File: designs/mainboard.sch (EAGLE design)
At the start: 11 parts, among them U1 ESP32-DEVKITC-32D

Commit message: changed schematic for display in eagle
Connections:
- new net N$4: U1.IO5
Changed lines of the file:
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@@
 <pinref part="U1" gate="G$1" pin="IO18"/>
 <wire x1="76.2" y1="50.8" x2="81.28" y2="50.8" width="0.1524" layer="91"/>
-<label x="81.28" y="50.8" size="1.778" layer="95"/>
+<label x="22.86" y="55.88" size="1.778" layer="95"/>
 </segment>
 </net>
@@
 <pinref part="U1" gate="G$1" pin="IO19"/>
 <wire x1="76.2" y1="53.34" x2="81.28" y2="53.34" width="0.1524" layer="91"/>
-<label x="81.28" y="53.34" size="1.778" layer="95"/>
+<label x="22.86" y="53.34" size="1.778" layer="95"/>
 </segment>
 </net>
@@
 <segment>
 <pinref part="U1" gate="G$1" pin="IO27"/>
-<label x="22.86" y="45.72" size="1.778" layer="95"/>
+<label x="22.86" y="48.26" size="1.778" layer="95"/>
 <wire x1="35.56" y1="45.72" x2="22.86" y2="45.72" width="0.1524" layer="91"/>
 </segment>
@@
 <segment>
 <pinref part="U1" gate="G$1" pin="IO26"/>
-<label x="22.86" y="48.26" size="1.778" layer="95"/>
+<label x="22.86" y="50.8" size="1.778" layer="95"/>
 <wire x1="35.56" y1="48.26" x2="22.86" y2="48.26" width="0.1524" layer="91"/>
 </segment>
@@
 <pinref part="U1" gate="G$1" pin="CLK"/>
 <wire x1="76.2" y1="25.4" x2="78.74" y2="25.4" width="0.1524" layer="91"/>
-<label x="22.86" y="53.34" size="1.778" layer="95"/>
+<label x="81.28" y="50.8" size="1.778" layer="95"/>
 </segment>
 <segment>
@@
 <pinref part="U1" gate="G$1" pin="SD0"/>
 <wire x1="76.2" y1="27.94" x2="78.74" y2="27.94" width="0.1524" layer="91"/>
-<label x="81.28" y="66.04" size="1.778" layer="95"/>
+<label x="81.28" y="68.58" size="1.778" layer="95"/>
 </segment>
 <segment>
@@
 <pinref part="U1" gate="G$1" pin="SD1"/>
 <wire x1="76.2" y1="30.48" x2="78.74" y2="30.48" width="0.1524" layer="91"/>
-<label x="81.28" y="68.58" size="1.778" layer="95"/>
+<label x="81.28" y="53.34" size="1.778" layer="95"/>
 </segment>
 <segment>
@@
 <pinref part="U1" gate="G$1" pin="IO32"/>
 <wire x1="35.56" y1="55.88" x2="22.86" y2="55.88" width="0.1524" layer="91"/>
-<label x="22.86" y="55.88" size="1.778" layer="95"/>
+<label x="81.28" y="48.26" size="1.778" layer="95"/>
 </segment>
 <segment>
@@
 <segment>
 <pinref part="U1" gate="G$1" pin="IO25"/>
-<label x="22.86" y="50.8" size="1.778" layer="95"/>
+<label x="22.86" y="45.72" size="1.778" layer="95"/>
 <wire x1="35.56" y1="50.8" x2="22.86" y2="50.8" width="0.1524" layer="91"/>
 </segment>
@@
 </segment>
 </net>
+<net name="N$4" class="0">
+<segment>
+<pinref part="U1" gate="G$1" pin="IO5"/>
+<wire x1="76.2" y1="48.26" x2="81.28" y2="48.26" width="0.1524" layer="91"/>
+</segment>
+</net>

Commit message: updated mainboard schematic
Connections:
- new net AUDIO_RX: U1.IO15
- new net AUDIO_TX: U1.IO4
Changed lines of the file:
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@@
+</segment>
+</net>
+<net name="AUDIO_TX" class="0">
+<segment>
+<pinref part="U1" gate="G$1" pin="IO4"/>
+<wire x1="76.2" y1="40.64" x2="81.28" y2="40.64" width="0.1524" layer="91"/>
+<label x="81.28" y="40.64" size="1.778" layer="95"/>
+</segment>
+</net>
+<net name="AUDIO_RX" class="0">
+<segment>
+<pinref part="U1" gate="G$1" pin="IO15"/>
+<wire x1="76.2" y1="33.02" x2="81.28" y2="33.02" width="0.1524" layer="91"/>
+<label x="81.28" y="33.02" size="1.778" layer="95"/>
 </segment>
 </net>

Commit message: added Library for DFPlayerMini
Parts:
- added U2: ESP32-DEVKITC-32D, ESP32-DEVKITC-32D_2:ESP32-DEVKITC-32D
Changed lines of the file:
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@@
 <grid distance="0.1" unitdist="inch" unit="inch" style="lines" multiple="1" display="no" altdistance="0.01" altunitdist="inch" altunit="inch"/>
 <layers>
-<layer number="1" name="Top" color="4" fill="1" visible="no" active="no"/>
-<layer number="2" name="Route2" color="1" fill="3" visible="no" active="no"/>
-<layer number="3" name="Route3" color="4" fill="3" visible="no" active="no"/>
-<layer number="4" name="tKeepout" color="0" fill="1" visible="no" active="no"/>
-<layer number="5" name="Route5" color="4" fill="4" visible="no" active="no"/>
-<layer number="6" name="Route6" color="1" fill="8" visible="no" active="no"/>
-<layer number="7" name="Route7" color="4" fill="8" visible="no" active="no"/>
-<layer number="8" name="Route8" color="1" fill="2" visible="no" active="no"/>
-<layer number="9" name="Route9" color="4" fill="2" visible="no" active="no"/>
-<layer number="10" name="Route10" color="1" fill="7" visible="no" active="no"/>
-<layer number="11" name="Route11" color="4" fill="7" visible="no" active="no"/>
-<layer number="12" name="Route12" color="1" fill="5" visible="no" active="no"/>
-<layer number="13" name="Route13" color="4" fill="5" visible="no" active="no"/>
-<layer number="14" name="Route14" color="1" fill="6" visible="no" active="no"/>
-<layer number="15" name="Route15" color="4" fill="6" visible="no" active="no"/>
-<layer number="16" name="Bottom" color="1" fill="1" visible="no" active="no"/>
-<layer number="17" name="Pads" color="2" fill="1" visible="no" active="no"/>
-<layer number="18" name="Vias" color="2" fill="1" visible="no" active="no"/>
-<layer number="19" name="Unrouted" color="6" fill="1" visible="no" active="no"/>
-<layer number="20" name="Dimension" color="15" fill="1" visible="no" active="no"/>
-<layer number="21" name="tPlace" color="7" fill="1" visible="no" active="no"/>
-<layer number="22" name="bPlace" color="7" fill="1" visible="no" active="no"/>
-<layer number="23" name="tOrigins" color="15" fill="1" visible="no" active="no"/>
-<layer number="24" name="bOrigins" color="15" fill="1" visible="no" active="no"/>
-<layer number="25" name="tNames" color="7" fill="1" visible="no" active="no"/>
-<layer number="26" name="bNames" color="7" fill="1" visible="no" active="no"/>
-<layer number="27" name="tValues" color="7" fill="1" visible="no" active="no"/>
-<layer number="28" name="bValues" color="7" fill="1" visible="no" active="no"/>
+<layer number="1" name="Top" color="4" fill="1" visible="yes" active="no"/>
+<layer number="2" name="Route2" color="1" fill="3" visible="yes" active="no"/>
+<layer number="3" name="Route3" color="4" fill="3" visible="yes" active="no"/>
+<layer number="4" name="tKeepout" color="0" fill="1" visible="yes" active="no"/>
+<layer number="5" name="Route5" color="4" fill="4" visible="yes" active="no"/>
+<layer number="6" name="Route6" color="1" fill="8" visible="yes" active="no"/>
+<layer number="7" name="Route7" color="4" fill="8" visible="yes" active="no"/>
+<layer number="8" name="Route8" color="1" fill="2" visible="yes" active="no"/>
+<layer number="9" name="Route9" color="4" fill="2" visible="yes" active="no"/>
+<layer number="10" name="Route10" color="1" fill="7" visible="yes" active="no"/>
+<layer number="11" name="Route11" color="4" fill="7" visible="yes" active="no"/>
+<layer number="12" name="Route12" color="1" fill="5" visible="yes" active="no"/>
+<layer number="13" name="Route13" color="4" fill="5" visible="yes" active="no"/>
+<layer number="14" name="Route14" color="1" fill="6" visible="yes" active="no"/>
+<layer number="15" name="Route15" color="4" fill="6" visible="yes" active="no"/>
+<layer number="16" name="Bottom" color="1" fill="1" visible="yes" active="no"/>
+<layer number="17" name="Pads" color="2" fill="1" visible="yes" active="no"/>
+<layer number="18" name="Vias" color="2" fill="1" visible="yes" active="no"/>
+<layer number="19" name="Unrouted" color="6" fill="1" visible="yes" active="no"/>
+<layer number="20" name="Dimension" color="15" fill="1" visible="yes" active="no"/>
+<layer number="21" name="tPlace" color="7" fill="1" visible="yes" active="no"/>
+<layer number="22" name="bPlace" color="7" fill="1" visible="yes" active="no"/>
+<layer number="23" name="tOrigins" color="15" fill="1" visible="yes" active="no"/>
+<layer number="24" name="bOrigins" color="15" fill="1" visible="yes" active="no"/>
+<layer number="25" name="tNames" color="7" fill="1" visible="yes" active="no"/>
+<layer number="26" name="bNames" color="7" fill="1" visible="yes" active="no"/>
+<layer number="27" name="tValues" color="7" fill="1" visible="yes" active="no"/>
+<layer number="28" name="bValues" color="7" fill="1" visible="yes" active="no"/>
 <layer number="29" name="tStop" color="7" fill="3" visible="no" active="no"/>
 <layer number="30" name="bStop" color="7" fill="6" visible="no" active="no"/>
@@
 <layer number="35" name="tGlue" color="7" fill="4" visible="no" active="no"/>
 <layer number="36" name="bGlue" color="7" fill="5" visible="no" active="no"/>
-<layer number="37" name="tTest" color="7" fill="1" visible="no" active="no"/>
-<layer number="38" name="bTest" color="7" fill="1" visible="no" active="no"/>
+<layer number="37" name="tTest" color="7" fill="1" visible="yes" active="no"/>
+<layer number="38" name="bTest" color="7" fill="1" visible="yes" active="no"/>
 <layer number="39" name="tKeepout" color="4" fill="11" visible="no" active="no"/>
 <layer number="40" name="bKeepout" color="1" fill="11" visible="no" active="no"/>
@@
 <layer number="44" name="Drills" color="7" fill="1" visible="no" active="no"/>
 <layer number="45" name="Holes" color="7" fill="1" visible="no" active="no"/>
-<layer number="46" name="Milling" color="3" fill="1" visible="no" active="no"/>
-<layer number="47" name="Measures" color="7" fill="1" visible="no" active="no"/>
-<layer number="48" name="Document" color="7" fill="1" visible="no" active="no"/>
-<layer number="49" name="Reference" color="7" fill="1" visible="no" active="no"/>
-<layer number="51" name="tDocu" color="7" fill="1" visible="no" active="no"/>
-<layer number="52" name="bDocu" color="7" fill="1" visible="no" active="no"/>
+<layer number="46" name="Milling" color="3" fill="1" visible="yes" active="no"/>
+<layer number="47" name="Measures" color="7" fill="1" visible="yes" active="no"/>
+<layer number="48" name="Document" color="7" fill="1" visible="yes" active="no"/>
+<layer number="49" name="Reference" color="7" fill="1" visible="yes" active="no"/>
+<layer number="51" name="tDocu" color="7" fill="1" visible="yes" active="no"/>
+<layer number="52" name="bDocu" color="7" fill="1" visible="yes" active="no"/>
 <layer number="88" name="SimResults" color="9" fill="1" visible="yes" active="yes"/>
 <layer number="89" name="SimProbes" color="9" fill="1" visible="yes" active="yes"/>
@@
 <part name="R6" library="rcl" library_urn="urn:adsk.eagle:library:334" deviceset="R-EU_" device="0204/7" package3d_urn="urn:adsk.eagle:package:23498/2" value="1k"/>
 <part name="SV1" library="con-lstb" library_urn="urn:adsk.eagle:library:162" deviceset="MA13-1" device="" package3d_urn="urn:adsk.eagle:package:8367/1"/>
+<part name="U2" library="ESP32-DEVKITC-32D_2" deviceset="ESP32-DEVKITC-32D" device="">
+<attribute name="SPICEPREFIX" value="X"/>
+</part>
 </parts>
 <sheets>
@@
 <attribute name="NAME" x="-19.05" y="41.402" size="1.778" layer="95"/>
 </instance>
+<instance part="U2" gate="G$1" x="-88.9" y="109.22" smashed="yes"/>
 </instances>
 <busses>

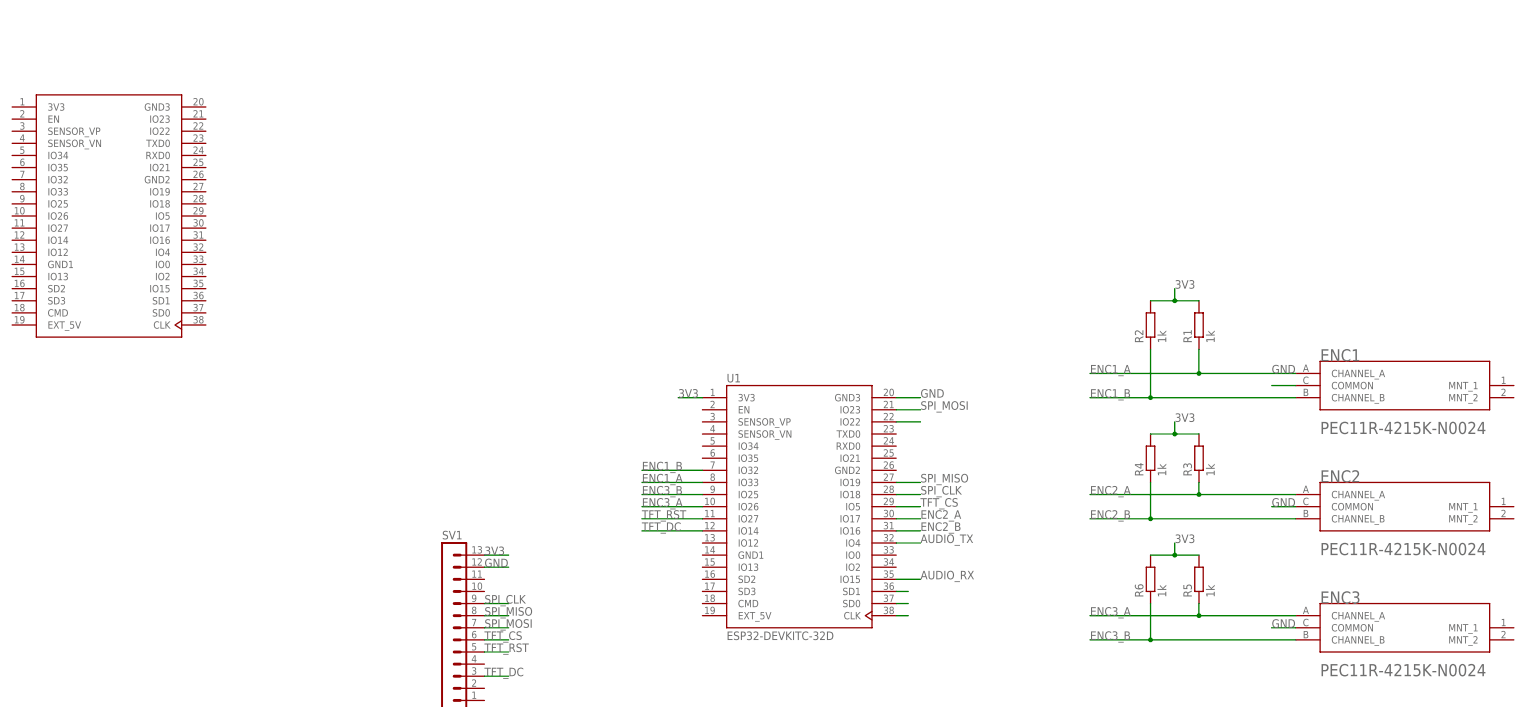
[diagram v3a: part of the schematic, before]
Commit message: added DFPlayer to mainboard schematic
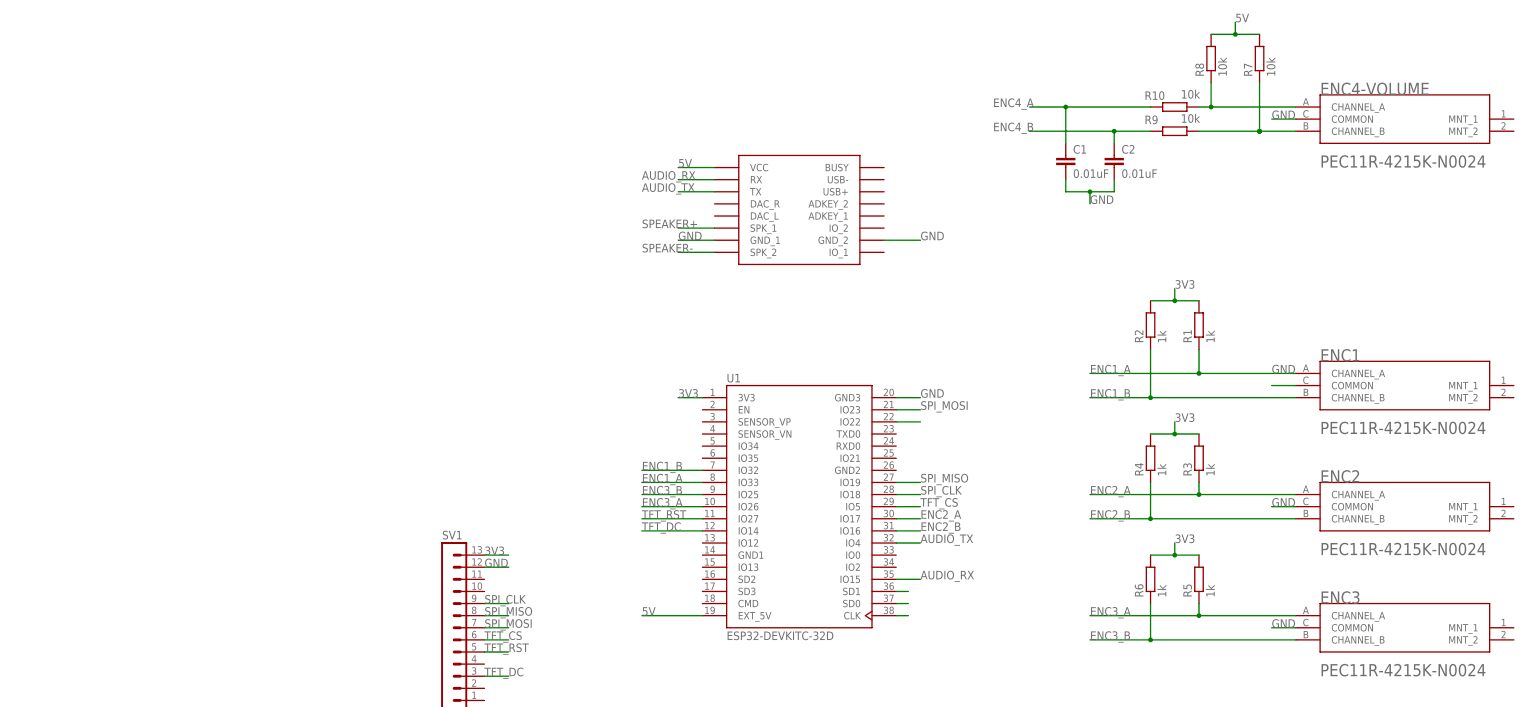
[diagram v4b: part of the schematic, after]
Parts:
- removed U2: ESP32-DEVKITC-32D, ESP32-DEVKITC-32D_2:ESP32-DEVKITC-32D
- added C1, C2: 0.01uF, capacitor-wima:C2,5-3
- added ENC4-VOLUME: BOURNS_PEC11R-4215K-N0024BOURNS_PEC11R-4215K-N0024_0_0, Bourns - PEC11R-4215K-N0024:BOURNS_PEC11R-4215K-N0024BOURNS_PEC11R-4215K-N0024_0_0
- added R10, R7, R8, R9: 10k, rcl:R-EU_0204/7
- added U$1: DFPLAYER, DFPlayer_v1:DFPLAYER
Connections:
- new net 5V: R7.2, R8.2, U$1.VCC, U1.EXT_5V
- new net ENC4_A: C1.1, R10.1
- new net ENC4_B: C2.1, R9.1
- new net N$5: ENC4-VOLUME.CHANNEL_A, R10.2, R8.1
- new net N$6: ENC4-VOLUME.CHANNEL_B, R7.1, R9.2
- new net SPEAKER+: U$1.SPK_1
- new net SPEAKER-: U$1.SPK_2
- net AUDIO_RX: now also U$1.RX
- net AUDIO_TX: now also U$1.TX
- net GND: now also C1.2, C2.2, ENC4-VOLUME.COMMON, U$1.GND_1, U$1.GND_2

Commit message: added additional encoders and connected them to the ESP
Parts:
- removed ENC1, ENC2, ENC3: BOURNS_PEC11R-4215K-N0024BOURNS_PEC11R-4215K-N0024_0_0, Bourns - PEC11R-4215K-N0024:BOURNS_PEC11R-4215K-N0024BOURNS_PEC11R-4215K-N0024_0_0
- added C10, C3, C4, C5, C6, C7, C8, C9: 0.01uF, capacitor-wima:C2,5-3
- added ENCODER1, ENCODER2, ENCODER3, ENCODER_ANTENNA: BOURNS_PEC11R-4215K-N0024BOURNS_PEC11R-4215K-N0024_0_0, Bourns - PEC11R-4215K-N0024:BOURNS_PEC11R-4215K-N0024BOURNS_PEC11R-4215K-N0024_0_0
- added R11, R12, R13, R14, R15, R16, R17, R18, R19, R20: 10k, rcl:R-EU_0204/7
- R1, R2, R3, R4, R5, R6: value 1k -> 10k
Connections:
- removed net ENC4_A: C1.1, R10.1
- removed net ENC4_B: C2.1, R9.1
- new net 3.3V: R1.2, R13.2, R14.2, R17.2, R18.2, R2.2, R3.2, R4.2, R7.2, R8.2
- new net ENCVOL_A: C1.1, R10.1, U1.IO22
- new net ENCVOL_B: C2.1, R9.1, U1.IO21
- new net ENC_ANT_A: C9.1, R6.1, U1.IO35
- new net ENC_ANT_B: C10.1, R5.1, U1.IO34
- new net N$11: ENCODER1.CHANNEL_A, R14.1, R16.2
- new net N$12: ENCODER1.CHANNEL_B, R13.1, R15.2
- new net N$14: ENCODER3.CHANNEL_A, R18.1, R20.2
- new net N$15: ENCODER3.CHANNEL_B, R17.1, R19.2
- new net N$17: ENCODER_ANTENNA.CHANNEL_B, R3.1, R5.2
- net 3V3: no longer R5.2, R6.2
- net 5V: no longer R7.2, R8.2
- net ENC1_A: now also C3.1, R16.1; no longer ENC1.CHANNEL_A, R1.1
- net ENC1_B: now also C4.1, R15.1; no longer ENC1.CHANNEL_B, R2.1
- net ENC2_A: now also C5.1, R12.1; no longer ENC2.CHANNEL_A, R3.1
- net ENC2_B: now also C6.1, R11.1; no longer ENC2.CHANNEL_B, R4.1
- net ENC3_A: now also C7.1, R20.1; no longer ENC3.CHANNEL_A, R5.1
- net ENC3_B: now also C8.1, R19.1; no longer ENC3.CHANNEL_B, R6.1
- net GND: now also C10.2, C3.2, C4.2, C5.2, C6.2, C7.2, C8.2, C9.2, ENCODER1.COMMON, ENCODER2.COMMON, ENCODER3.COMMON, ENCODER_ANTENNA.COMMON; no longer ENC1.COMMON, ENC2.COMMON, ENC3.COMMON
- net N$2: now also ENCODER2.CHANNEL_A, R12.2, R2.1; no longer U1.IO22
- net N$8: now also ENCODER_ANTENNA.CHANNEL_A, R4.1, R6.2; no longer R3.2, R4.2
- net N$9: now also ENCODER2.CHANNEL_B, R1.1, R11.2; no longer R1.2, R2.2
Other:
- moved on the sheet: R1, R2, R3, R4, R5, R6
